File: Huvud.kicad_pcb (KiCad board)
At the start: 4 copper layers, 42 x 42 mm, 117 parts, among them J10 Probe, J2 DBG, J3 THERM, J4 FAN0, J5 FAN1, J6 Heater, J7 Endstop, J9 STEPPER, Q1 AO3400A, Q2 AO3400A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

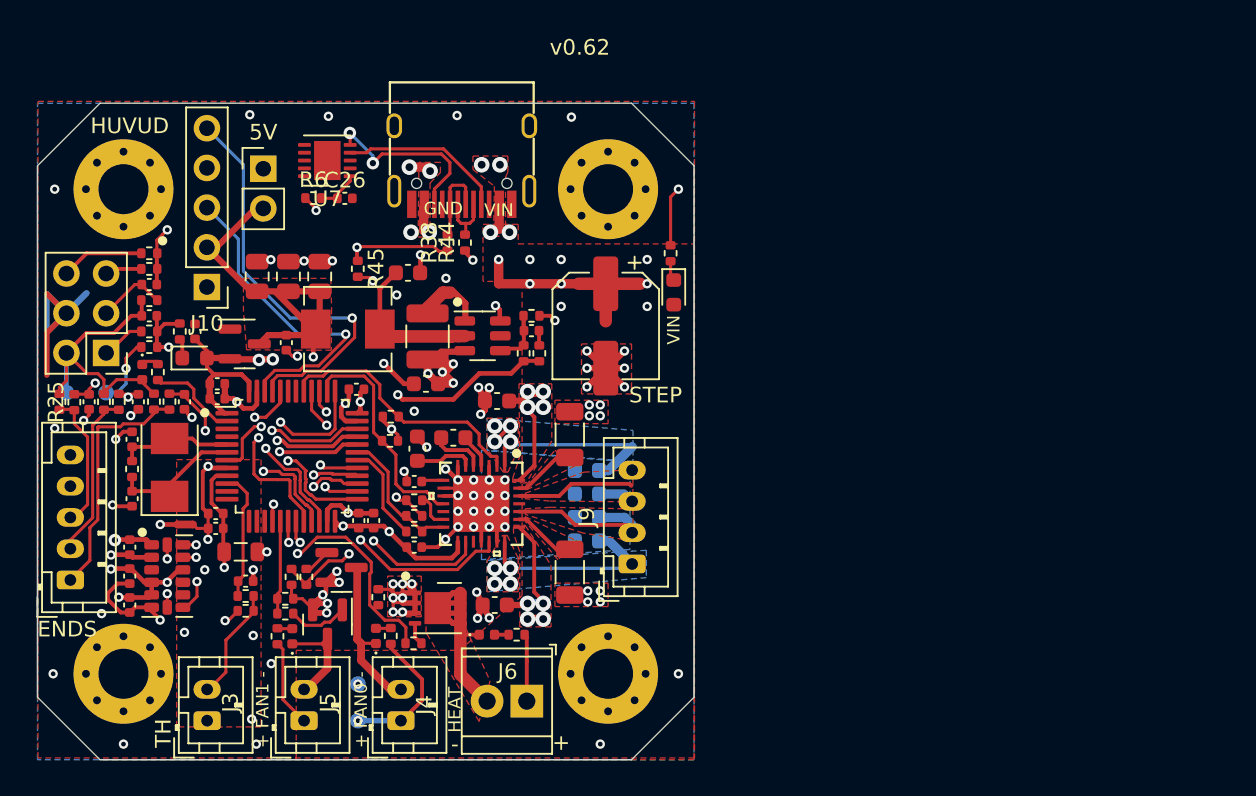
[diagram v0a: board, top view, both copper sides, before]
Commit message: repace TMC2209 with module
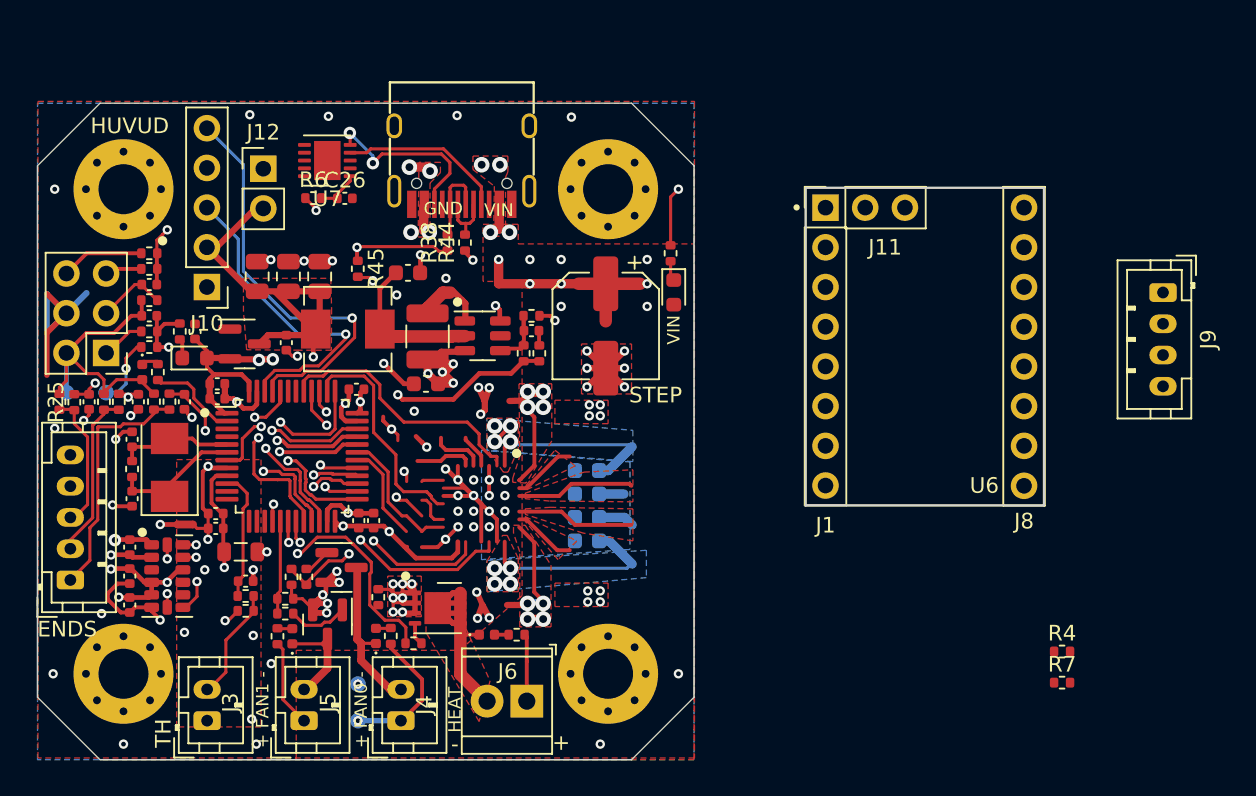
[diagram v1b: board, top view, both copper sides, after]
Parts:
- removed C3, C6, C7: 0.1uF/35V, Capacitor_SMD:C_0603_1608Metric
- removed C4: 4.7uF, Capacitor_SMD:C_0402_1005Metric
- removed C5: 22nf/50V, Capacitor_SMD:C_0603_1608Metric
- removed C9: 0.1uF, Capacitor_SMD:C_0402_1005Metric
- removed R16: 1k, Resistor_SMD:R_0402_1005Metric
- removed R17, R18, R24, R39: 22k, Resistor_SMD:R_0402_1005Metric
- removed U2: TMC2209-LA, TMC2209:TMC2209-LA
- added J1: TMC2209_BIGTREETECH_V1.2_HEADER_1, Huvud:HEADER_TMC2209_BIGTREETECH_1, F.Cu at (238.8, 115.6)
- added J11: TMC2209_BIGTREETECH_V1.2_HEADER_3, Huvud:HEADER_TMC2209_BIGTREETECH_3, F.Cu at (238.8, 115.6)
- added J8: TMC2209_BIGTREETECH_V1.2_HEADER_2, Huvud:HEADER_TMC2209_BIGTREETECH_2, F.Cu at (238.8, 115.6)
- added U6: TMC2209_BIGTREETECH_V1.2_MODULE, Huvud:MODULE_TMC2209_BIGTREETECH, F.Cu at (238.8, 115.6)
- R4: value 0.110 1% -> 22k; footprint Resistor_SMD:R_1206_3216Metric -> Resistor_SMD:R_0402_1005Metric
- R7: value 0.110 1% -> 1k; footprint Resistor_SMD:R_1206_3216Metric -> Resistor_SMD:R_0402_1005Metric
- moved J9 38.1 mm to (254.0, 112.1), turned to -90 degrees
- moved R7 35.3 mm to (247.5, 137.1), turned to 0 degrees
- moved R4 31.9 mm to (247.5, 135.1), turned to 0 degrees
- renumbered 5V to J12
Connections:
- R4 pad 1: GND -> ST_DIAG
- R4 pad 2: BRA -> +3V3
- R7 pad 1: GND -> ST_UART_TX
- R7 pad 2: BRB -> ST_UART_RX
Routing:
- net (no net): track 0.00 -> 21.3 mm
- net BRB: track 4.08 -> 0.00 mm
- net BRA: track 4.05 -> 0.00 mm
- net Net-(U2-VCP): track 3.74 -> 0.00 mm
- net Net-(U2-CPI): track 3.47 -> 0.00 mm
- net Net-(U2-CLK): track 2.31 -> 0.00 mm
- net Net-(U2-CPO): track 2.21 -> 0.00 mm
- net Net-(U2-5VOUT): track 1.41 -> 0.00 mm
- added copper zone on F.Cu, net (none)
- removed copper zone on F.Cu, net BRA
- removed copper zone on F.Cu, net BRB
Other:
- board text removed: "v0.62"

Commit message: re-layout
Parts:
- C37, C38, C39, C40: moved to F.Cu
- moved R4 48.5 mm to (202.4, 117.3)
- moved R7 43.5 mm to (207.0, 121.3), turned to 90 degrees
- moved J9 32.2 mm to (222.2, 117.6)
- moved J1 27.9 mm to (211.3, 120.7)
- moved J11 27.9 mm to (211.3, 120.7)
- moved J8 27.9 mm to (211.3, 120.7)
- moved U6 27.9 mm to (211.3, 120.7)
- moved C38 14.7 mm to (220.3, 113.7), turned to -90 degrees
- moved C8 14.4 mm to (211.3, 126.9), turned to 180 degrees
- moved R41 8.86 mm to (211.2, 122.1), turned to 90 degrees
- moved C37 8.52 mm to (215.6, 118.1), turned to -90 degrees
- moved R29 8.48 mm to (208.8, 122.6), turned to 180 degrees
- moved C21 8.28 mm to (210.3, 122.1), turned to -90 degrees
- moved C20 7.95 mm to (212.6, 114.8), turned to 90 degrees
- moved R40 7.08 mm to (208.8, 121.6), turned to 180 degrees
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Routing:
- net ST_VS: track 81.7 -> 52.6 mm, vias 34 -> 28
- net GND: track 128.3 -> 101.9 mm, vias 89 -> 51
- net (no net): track 21.3 -> 0.00 mm
- net +3V3: track 96.1 -> 116.8 mm, vias 9 -> 7
- net Net-(U3-SW): track 10.1 -> 19.0 mm
- net ST_EN: track 17.0 -> 9.88 mm, vias 0 -> 1
- net ST_DIR: track 20.9 -> 13.8 mm
- net ST_STEP: track 18.6 -> 12.6 mm
- net ST_A2: track 16.4 -> 12.5 mm, vias 4 -> 0
- net Net-(U3-BOOT): track 8.77 -> 12.0 mm
- net ST_B2: track 15.7 -> 12.6 mm, vias 4 -> 0
- net ST_B1: track 9.13 -> 12.1 mm
- net PROBE_SERVO: track 20.8 -> 18.4 mm
- net ST_A1: track 9.83 -> 12.2 mm
- net +5V: track 41.4 -> 39.2 mm
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- removed copper zone on F.Cu, net (none)
- removed copper zone on F.Cu, net ST_A1
- removed copper zone on B.Cu, net ST_A2
- removed copper zone on F.Cu, net ST_A2
- removed copper zone on F.Cu, net ST_B1
- removed copper zone on B.Cu, net ST_B2
- removed copper zone on F.Cu, net ST_B2
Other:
- board text added: "Probe"
- board text added: "S"
- board text removed: "H"
- board text removed: "HUVUD"
- board text removed: "L"
- board text removed: "TH2"
- board text removed: "USB CAN"
- board text removed: "github.com/bondus/KlipperToolboard"

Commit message: cleanup and bom
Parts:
- moved C14 0.38 mm to (200.0, 110.0)
- moved C15 0.38 mm to (196.0, 110.0)
- moved C32 0.38 mm to (198.0, 110.0)
- moved J12 0.31 mm to (196.4, 103.9)
- moved R8 0.26 mm to (198.0, 130.3)
- moved R34 0.19 mm to (199.0, 130.3)
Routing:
- net +5V: track 39.2 -> 36.2 mm, vias 2 -> 7
- net GND: track 101.9 -> 99.4 mm
- net Net-(U5-PD1): track 9.29 -> 7.41 mm
- net +3V3: track 116.8 -> 115.3 mm
- net ST_A1: track 12.2 -> 10.8 mm
- net ST_VS: track 52.6 -> 51.6 mm
- net Net-(D3-K): track 15.6 -> 14.6 mm
- net Net-(U5-PD0): track 8.08 -> 7.32 mm
- net BOOT1: track 23.0 -> 22.4 mm
- net ST_B1: track 12.1 -> 11.5 mm
